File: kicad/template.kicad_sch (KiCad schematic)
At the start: 33 parts, among them J1 Bus_PCI_Express_x1, J2 Micro_SD_Card, J3 Conn_01x02_Pin, J6 USB_C_Receptacle_USB2.0_16P, U1 MCP25625T-E/ML, U2 RP2040, U4 W25Q128JVP, X1 ABM8-272-T3, Y1 X322516MLB4SI

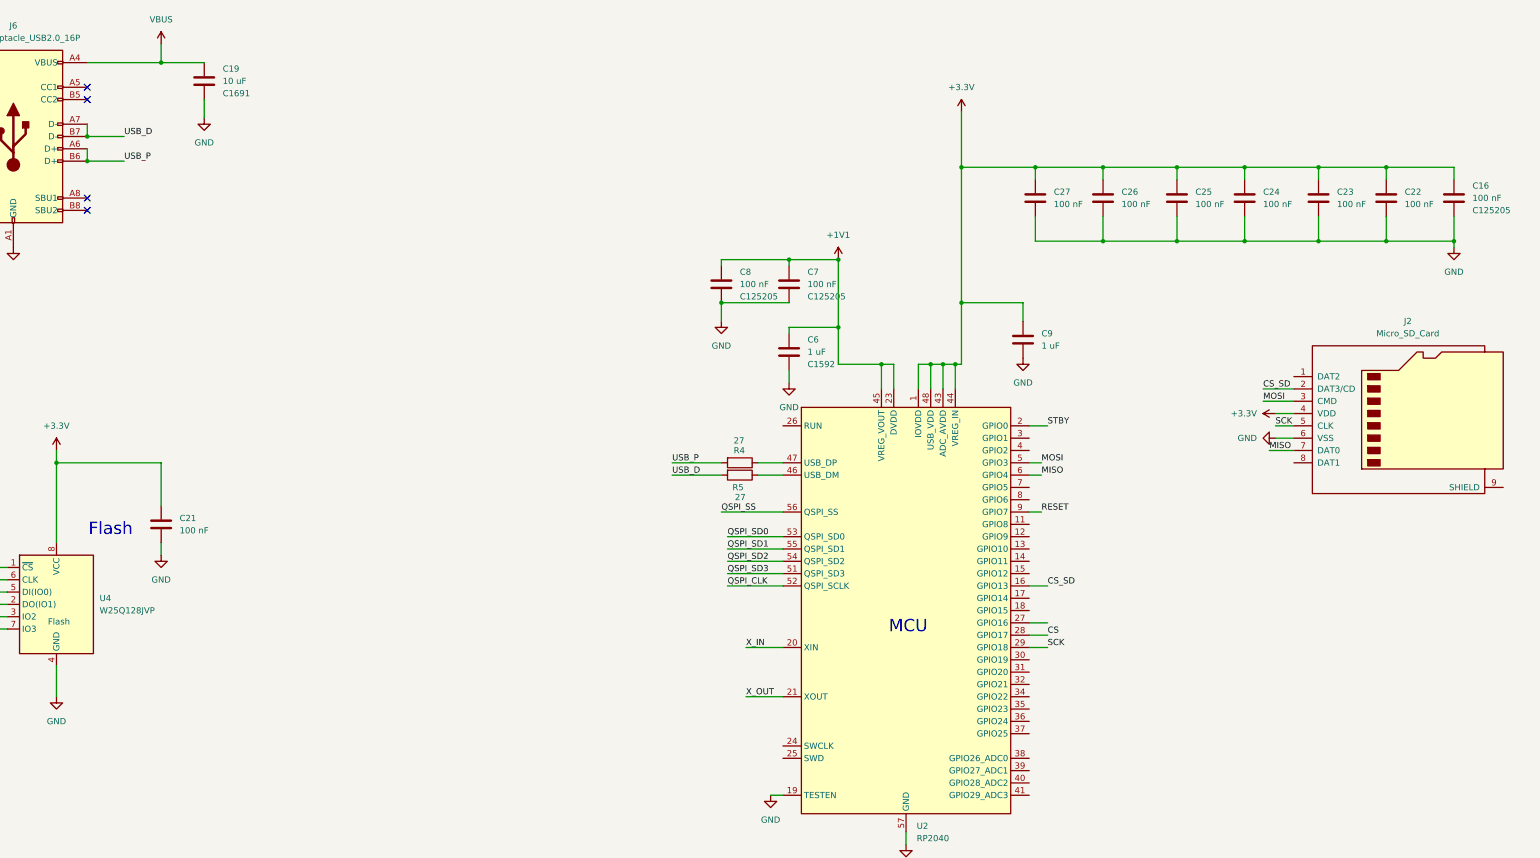
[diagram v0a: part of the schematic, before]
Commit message: update schematic
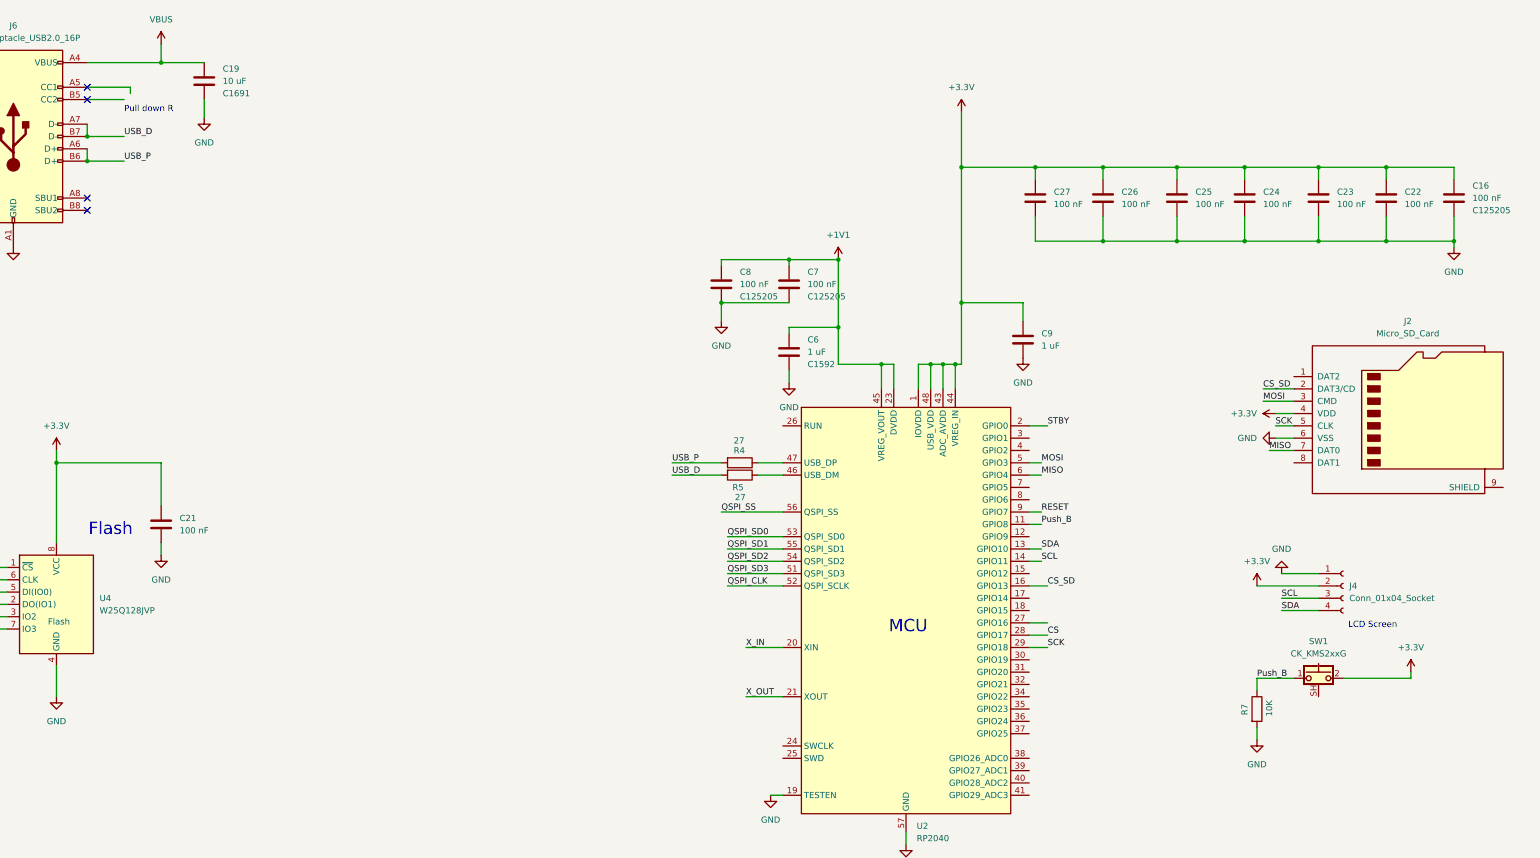
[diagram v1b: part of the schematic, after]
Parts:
- added J4: Conn_01x04_Socket, Connector_Hirose:Hirose_DF13-04P-1.25DSA_1x04_P1.25mm_Vertical, symbol Connector:Conn_01x04_Socket
- added R7: 10K, Resistor_SMD:R_0603_1608Metric, symbol Device:R
- added SW1: CK_KMS2xxG, Button_Switch_SMD:SW_SPST_CK_KMS2xxGP, symbol Switch:CK_KMS2xxG
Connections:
- net +3.3V: now also J4.2 (Pin_2), SW1.2
- net GND: now also J4.1 (Pin_1), R7.2
- net Push_B: now reaches U2.11 (GPIO8)
- net Push_B: now also R7.1, SW1.1
- net SDA: now reaches U2.13 (GPIO10)
- net SDA: now also J4.4 (Pin_4)
- net SCL: now reaches U2.14 (GPIO11)
- net SCL: now also J4.3 (Pin_3)
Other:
- note added: "LCD Screen"
- note added: "Pull down R"

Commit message: update schematic
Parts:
- removed J2: Micro_SD_Card, Connector_Card:microSD_HC_Wuerth_693072010801, symbol Connector:Micro_SD_Card
- removed J3: Conn_01x02_Pin, Connector_Hirose:Hirose_DF13-02P-1.25DSA_1x02_P1.25mm_Vertical, symbol Connector:Conn_01x02_Pin
- removed SW1: CK_KMS2xxG, Button_Switch_SMD:SW_SPST_CK_KMS2xxGP, symbol Switch:CK_KMS2xxG
- added J5: TF-115-BCP9, TF115BCP9, symbol TF-115-BCP9:TF-115-BCP9
- added R10, R8, R9: 10K, Resistor_SMD:R_0603_1608Metric, symbol Device:R
- added R11, R12: 5.1K, Resistor_SMD:R_0603_1608Metric, symbol Device:R
- added S1, S10, S2, S7, S8, S9: TS-1187A-B-A-B, Nicolas Library:SW_TS-1187A-B-A-B, symbol TS-1187A-B-A-B:TS-1187A-B-A-B
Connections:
- net Push_B is gone; now on net Push_B1: R7.1, U2.11 (GPIO8)
- net +3.3V: now also J5.4 (VDD), S7.C
- net CS_SD: now also J5.2 (CD/DAT3)
- net GND: now also J5.6 (VSS), J5.G1 (GND_1), J5.G2 (GND_2), J5.G3 (GND_3), J5.G4 (GND_4), R10.2, R11.1, R12.1, R8.2, R9.2, S1.A, S2.A
- net MISO: now also J5.7 (DAT0)
- net MOSI: now also J5.3 (CMD)
- net SCK: now also J5.5 (CLX)
- net ~{USB_BOOT_S}: now reaches R6.2
- net ~{USB_BOOT_S}: now also S1.C
- net at U2.26 (RUN): now also S2.C
- net Push_B1: now reaches U2.30 (GPIO19)
- net Push_B1: now also S7.A
- net Push_B2: now reaches U2.31 (GPIO20)
- net Push_B2: now also R8.1
- net Push_B3: now reaches U2.35 (GPIO23)
- net Push_B3: now also R9.1, S9.A
- net Push_B4: now reaches U2.36 (GPIO24)
- net Push_B4: now also R10.1, S10.A
- net at J6.A5 (CC1): now also R11.2
- net at J6.B5 (CC2): now also R12.2
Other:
- note added: "LCD2"
- note added: "LCD3"
- note added: "LCD4"
- note added: "Reboot"
- note added: "Reset PB"
- note removed: "Pull down R"

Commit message: update schematic
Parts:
- removed S1, S2: TS-1187A-B-A-B, Nicolas Library:SW_TS-1187A-B-A-B, symbol TS-1187A-B-A-B:TS-1187A-B-A-B
- added S11, S12: TS-1187A-B-A-B, Nicolas Library:SW_TS-1187A-B-A-B, symbol TS-1187A-B-A-B:TS-1187A-B-A-B
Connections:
- net GND: now also S11.A, S12.A
- net ~{USB_BOOT_S}: now also S12.C
- net at U2.26 (RUN): now also S11.C

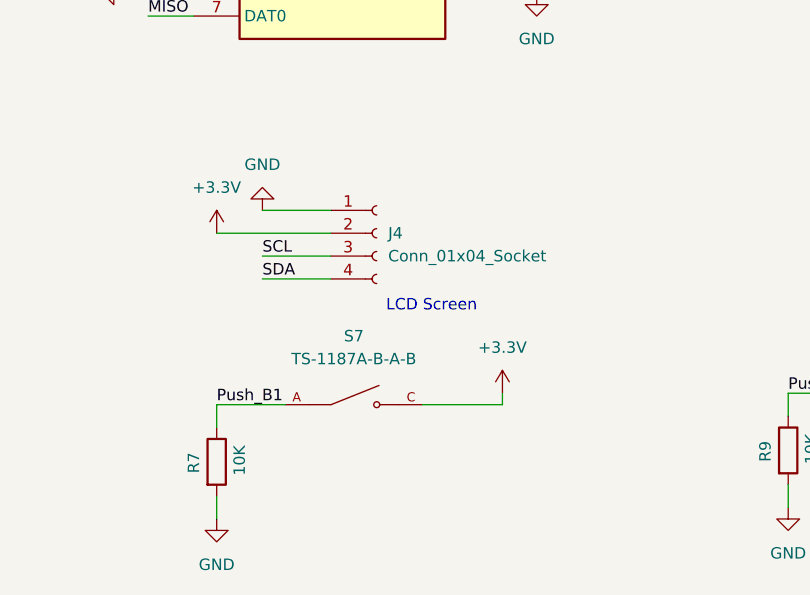
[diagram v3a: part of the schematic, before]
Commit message: update schematic
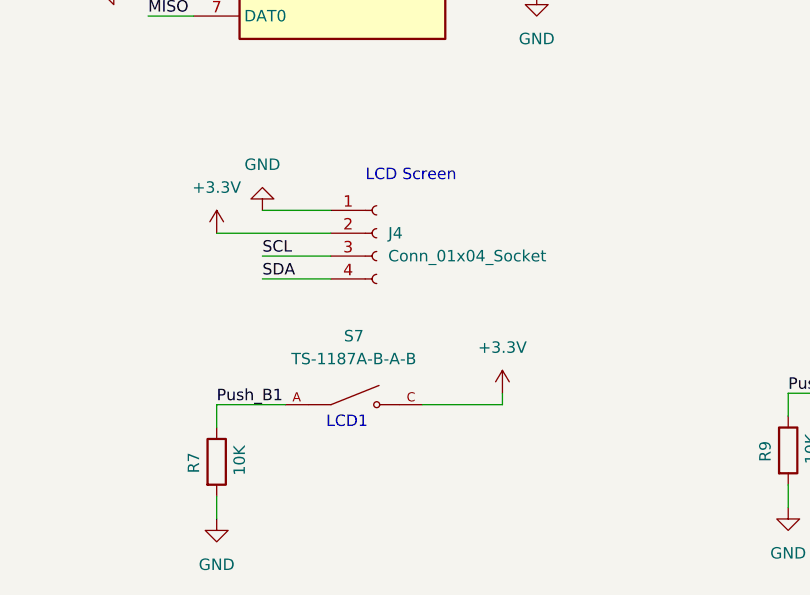
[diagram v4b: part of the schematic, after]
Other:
- note added: "LCD1"
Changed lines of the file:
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@@
+		)
+	)
+	(text "LCD1\n\n"
+		(exclude_from_sim no)
+		(at 387.858 196.088 0)
+		(effects
+			(font
+				(size 1.27 1.27)
+			)
 		)
 	)
@@
 	(text "LCD Screen\n"
 		(exclude_from_sim no)
-		(at 397.256 182.118 0)
+		(at 394.97 167.64 0)
 		(effects
 			(font

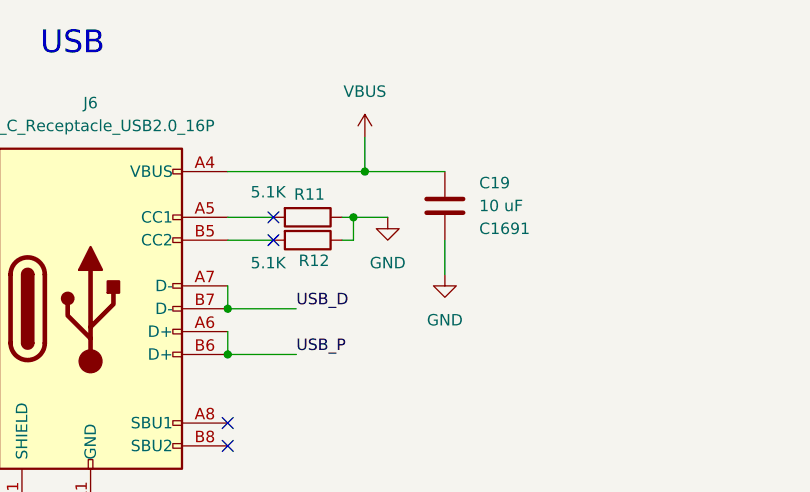
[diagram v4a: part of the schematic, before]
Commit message: update schematic
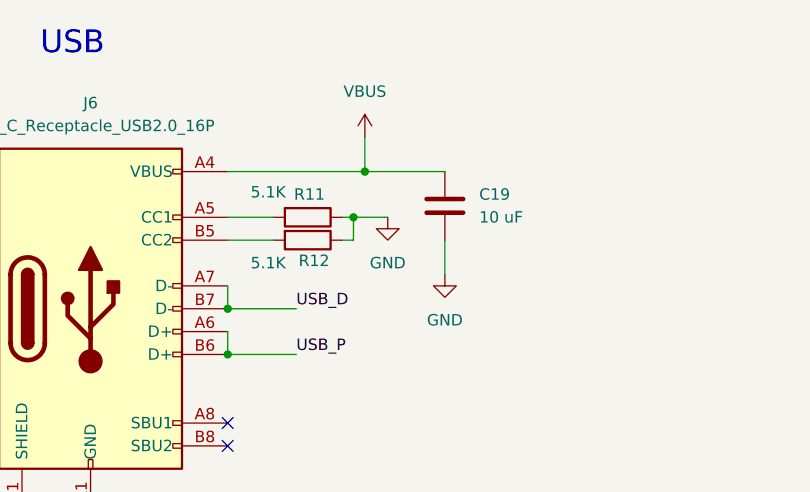
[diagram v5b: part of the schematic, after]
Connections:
- no-connect marks 9 -> 7
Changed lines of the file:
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@@
 	)
 	(no_connect
-		(at 137.16 73.66)
-	)
-	(no_connect
 		(at 60.96 346.71)
 	)
 	(no_connect
-		(at 137.16 71.12)
-	)
-	(no_connect
 		(at 60.96 275.59)
 	)
@@
 		(fields_autoplaced yes)
 		(property "Reference" "C19"
-			(at 160.02 67.3099 0)
+			(at 160.02 68.5799 0)
 			(effects
 				(font
@@
 		)
 		(property "Value" "10 uF"
-			(at 160.02 69.8499 0)
+			(at 160.02 71.1199 0)
 			(effects
 				(font
@@
 				)
 				(justify right)
+				(hide yes)
 			)
 		)

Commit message: Changed Schematic
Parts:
- removed J4: Conn_01x04_Socket, Connector_Hirose:Hirose_DF13-04P-1.25DSA_1x04_P1.25mm_Vertical, symbol Connector:Conn_01x04_Socket
- added J2: PPTC041LGBN-RC, Nicolas Library:CONN_PPTC041LGBN-RC_SUL, symbol 2025-05-16_00-29-22:PPTC041LGBN-RC
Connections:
- net +3.3V: now also J2.2
- net GND: now also J2.1
- net SCL: now also J2.3
- net SDA: now also J2.4

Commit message: Update PCB Layout
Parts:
- added R13: 10K, Resistor_SMD:R_0603_1608Metric, symbol Device:R
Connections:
- net +3.3V: now also R13.2
- net GND: now also U1.29 (EPAD)
- net RESET: now also R13.1
- net INT: now reaches U1.25 (*INT)
- net INT: now also U2.32 (GPIO21)
- net CANN renamed CANL
- net CANP renamed CANH
- net USB_D renamed USB_N
- no-connect marks 7 -> 10
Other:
- note added: "Boot"
- note removed: "Reboot"
- moved on the sheet: C1

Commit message: PCB Layout update
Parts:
- removed C1, C2: 0.1 uF, Capacitor_SMD:C_0603_1608Metric, symbol Device:C
- removed C19: 10 uF, Capacitor_SMD:C_0603_1608Metric, symbol Device:C
- removed C21, C24, C25, C26, C27: 100 nF, Capacitor_SMD:C_0603_1608Metric, symbol Device:C
- added C10, C11, C12, C13, C14, C15, C20: 100 nF, Capacitor_SMD:C_0402_1005Metric, symbol Device:C
- added J4: Conn_01x02, Connector_PinHeader_2.54mm:PinHeader_1x02_P2.54mm_Vertical, symbol Connector_Generic:Conn_01x02
- C16, C8: footprint Capacitor_SMD:C_0603_1608Metric -> Capacitor_SMD:C_0402_1005Metric; JLC Link https://jlcpcb.com/partdetail/TORCH-CT41G_0603_2X1_50V_0_1_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 -> https://jlcpcb.com/partdetail/291005-CL05B104KB54PNC/C307331; LCSC Part # C125205 -> C307331
- C17: value 15 pF -> 100 nF; footprint Capacitor_SMD:C_0603_1608Metric -> Capacitor_SMD:C_0402_1005Metric; JLC Link https://jlcpcb.com/partdetail/Yageo-CC0603JRNPO9BN150/C1070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 -> https://jlcpcb.com/partdetail/291005-CL05B104KB54PNC/C307331; LCSC Part # C107037 -> C307331
- C18: footprint Capacitor_SMD:C_0603_1608Metric -> Capacitor_SMD:C_0402_1005Metric; JLC Link https://jlcpcb.com/partdetail/Yageo-CC0603JRNPO9BN150/C1070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 -> https://jlcpcb.com/partdetail/1900-0402CG150J500NT/C1548; LCSC Part # C107037 -> C1548
- C22: value 100 nF -> 22 pF; footprint Capacitor_SMD:C_0603_1608Metric -> Capacitor_SMD:C_0402_1005Metric; JLC Link https://jlcpcb.com/partdetail/TORCH-CT41G_0603_2X1_50V_0_1_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 -> https://jlcpcb.com/partdetail/71561-CL05C220JB5NNNC/C70464; LCSC Part # C125205 -> C70464
- C23: value 100 nF -> 15 pF; footprint Capacitor_SMD:C_0603_1608Metric -> Capacitor_SMD:C_0402_1005Metric; JLC Link https://jlcpcb.com/partdetail/TORCH-CT41G_0603_2X1_50V_0_1_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 -> https://jlcpcb.com/partdetail/1900-0402CG150J500NT/C1548; LCSC Part # C125205 -> C1548
- C3: value 0.1 uF -> 100 nF; footprint Capacitor_SMD:C_0603_1608Metric -> Capacitor_SMD:C_0402_1005Metric; JLC Link https://jlcpcb.com/partdetail/1942-CL10B104KA8NNNC/C1590 -> https://jlcpcb.com/partdetail/291005-CL05B104KB54PNC/C307331; LCSC Part # C1590 -> C307331
- C4, C5: value 0.22 uF -> 100 nF; footprint Capacitor_SMD:C_0603_1608Metric -> Capacitor_SMD:C_0402_1005Metric; JLC Link https://jlcpcb.com/partdetail/1958-0603B224K250NT/C1606 -> https://jlcpcb.com/partdetail/291005-CL05B104KB54PNC/C307331; LCSC Part # C1606 -> C307331
- C6: value 1 uF -> 22 pF; footprint Capacitor_SMD:C_0603_1608Metric -> Capacitor_SMD:C_0402_1005Metric; JLC Link https://jlcpcb.com/partdetail/1944-CL10A105KO8NNNC/C1592 -> https://jlcpcb.com/partdetail/71561-CL05C220JB5NNNC/C70464; LCSC Part # C1592 -> C70464
- C7: value 100 nF -> 1 uF; footprint Capacitor_SMD:C_0603_1608Metric -> Capacitor_SMD:C_0402_1005Metric; JLC Link https://jlcpcb.com/partdetail/TORCH-CT41G_0603_2X1_50V_0_1_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 -> https://jlcpcb.com/partdetail/53938-CL05A105KA5NQNC/C52923; LCSC Part # C125205 -> C52923
- C9: footprint Capacitor_SMD:C_0603_1608Metric -> Capacitor_SMD:C_0402_1005Metric; JLC Link https://jlcpcb.com/partdetail/1944-CL10A105KO8NNNC/C1592 -> https://jlcpcb.com/partdetail/53938-CL05A105KA5NQNC/C52923; LCSC Part # C1592 -> C52923
- R10, R13, R7, R8, R9: footprint Resistor_SMD:R_0603_1608Metric -> Resistor_SMD:R_0402_1005Metric; JLC Link https://jlcpcb.com/partdetail/Vo-0603_5_1K/C2889391 -> https://jlcpcb.com/partdetail/Yageo-RC0402JR0710KL/C60489; LCSC Part # C2889391 -> C60489
- R11, R12: footprint Resistor_SMD:R_0603_1608Metric -> Resistor_SMD:R_0402_1005Metric; JLC Link https://jlcpcb.com/partdetail/Yageo-RC0603JR075K1L/C14677 -> https://jlcpcb.com/partdetail/26648-0402WGF5101TCE/C25905; LCSC Part # C14677 -> C25905
- R3, R6: footprint Resistor_SMD:R_0603_1608Metric -> Resistor_SMD:R_0402_1005Metric; JLC Link https://jlcpcb.com/partdetail/Vo-0603_5_1K/C2889391 -> https://jlcpcb.com/partdetail/12256-0402WGF1001TCE/C11702; LCSC Part # C2889391 -> C11702
- R4, R5: footprint Resistor_SMD:R_0603_1608Metric -> Resistor_SMD:R_0402_1005Metric; JLC Link https://jlcpcb.com/partdetail/25933-0603WAF270JT5E/C25190 -> https://jlcpcb.com/partdetail/25843-0402WGF270JTCE/C25100; LCSC Part # C25190 -> C25100
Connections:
- net +1V1: now also C9.2, C10.2; no longer C6.2, C7.2
- net +3.3V: now also C17.2, C4.1, C5.1, C7.2, R13.1, C11.2, C12.2, C13.2, C14.2, C15.2, C20.2; no longer C22.2, C23.2, C9.2, R13.2
- net GND: now also C17.1, C23.2, C4.2, C5.2, C10.1, C11.1, C12.1, C13.1, C14.1, C15.1, C20.1; no longer C17.2, C23.1, C4.1, C5.1
- net OSC1: now also C22.2; no longer C5.2
- net OSC2: now also C6.2; no longer C4.2
- net Push_B1: no longer U2.11 (GPIO8)
- net Push_B2: now also R10.1, S8.A; no longer R8.1
- net Push_B3: now also R8.1; no longer R9.1
- net Push_B4: now also R9.1; no longer R10.1
- net RESET: now also R13.2; no longer R13.1
- net X_IN: now also C23.1; no longer C17.1
- net SWCLK: now reaches U2.24 (SWCLK)
- net SWCLK: now also J4.1 (Pin_1)
- net SWD: now reaches U2.25 (SWD)
- net SWD: now also J4.2 (Pin_2)
- net VBUS: no longer names the net of J6.A4 (VBUS), J6.A9 (VBUS), J6.B4 (VBUS), J6.B9 (VBUS)
- no-connect marks 10 -> 17
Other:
- moved on the sheet: S8
